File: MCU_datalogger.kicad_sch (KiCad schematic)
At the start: 25 parts, among them U1 24LC1025, U2 24LC1025, U3 DS1337S_, U4 ATMEGA328P-AU, Y1 32.768 KHz, Y2 16 MHz

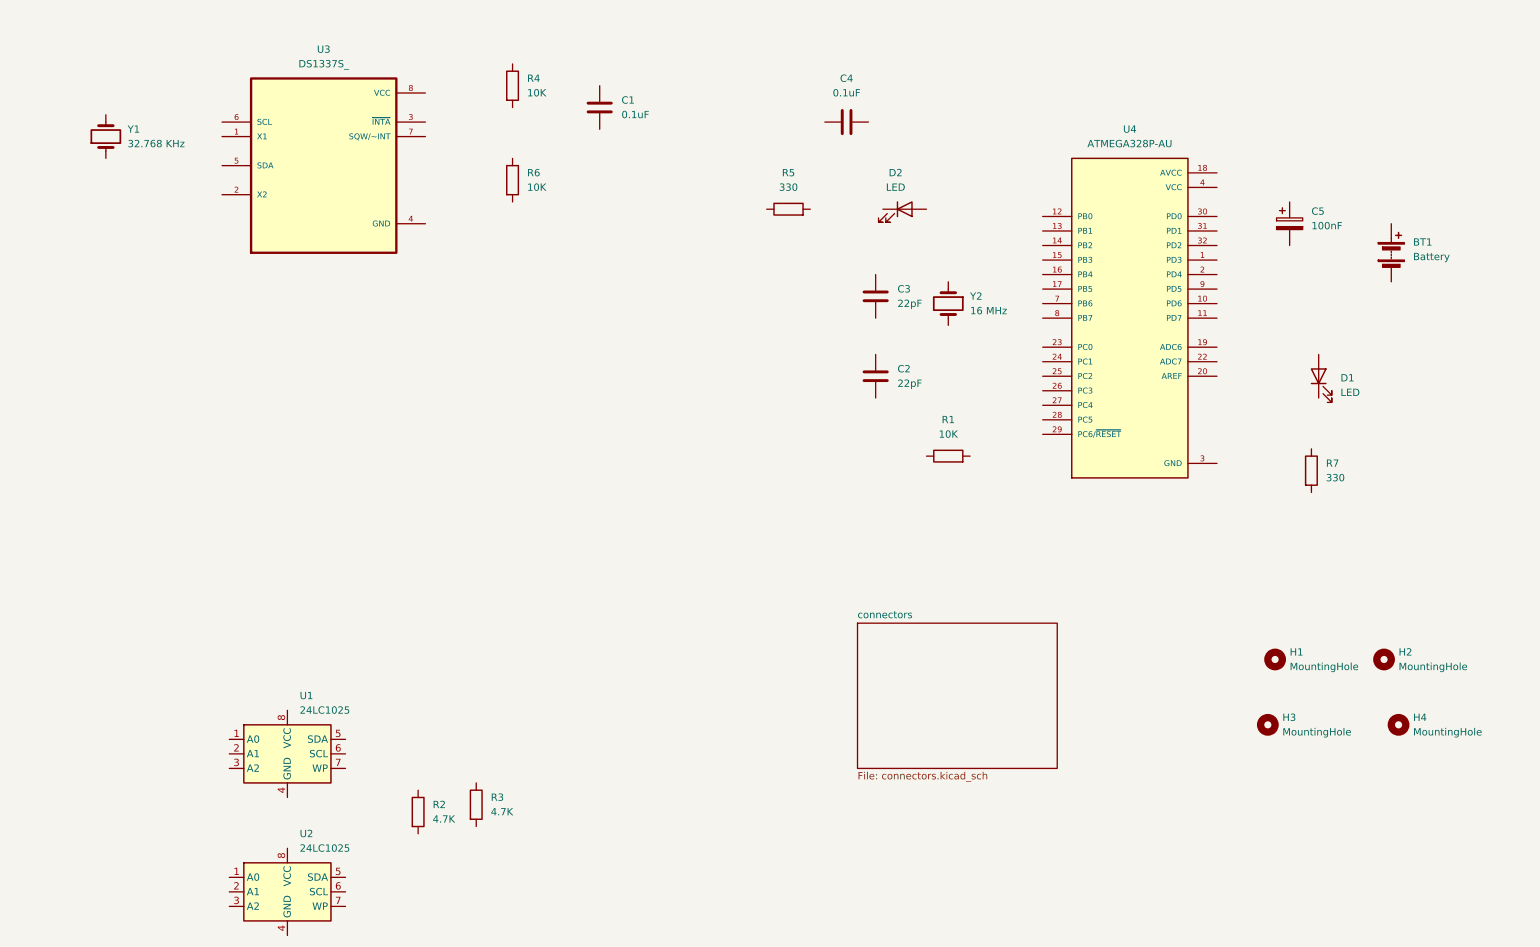
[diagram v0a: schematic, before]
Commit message: finished wiring main sheet
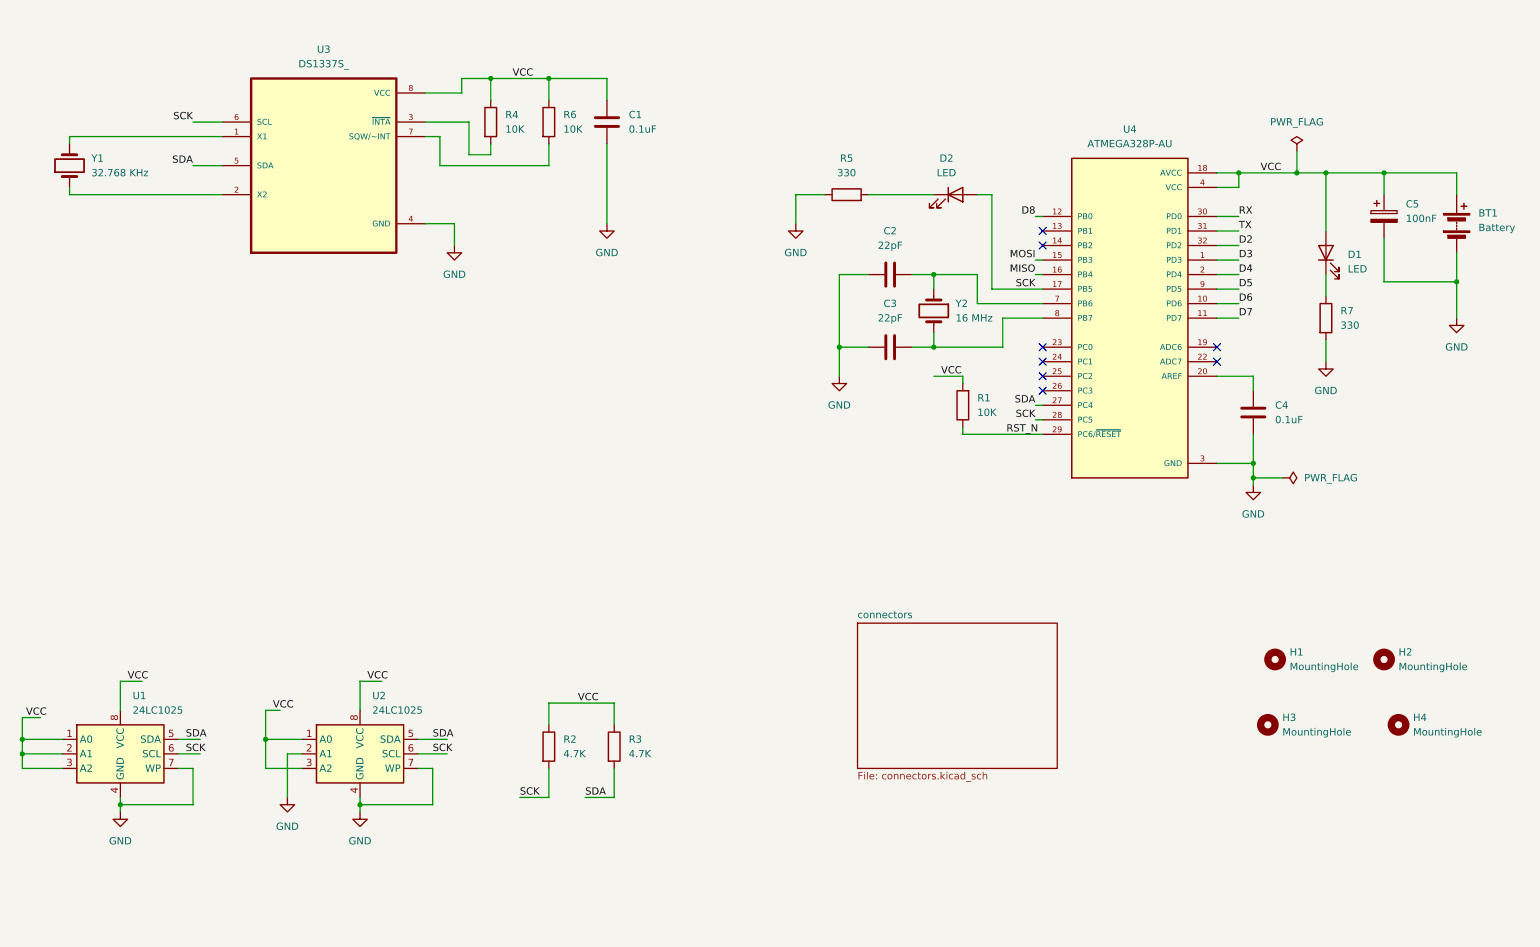
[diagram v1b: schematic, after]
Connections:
- net GND: now also BT1.2 (-), C1.2, C2.1, C3.1, C4.1, C5.2, R5.1, R7.2, U1.4 (GND), U1.7 (WP), U2.2 (A1), U2.4 (GND), U2.7 (WP), U3.4 (GND)
- net VCC: now also BT1.1 (+), C1.1, C5.1, D1.2 (A), R1.2, R2.1, R3.1, R4.1, R6.1, U1.1 (A0), U1.2 (A1), U1.3 (A2), U1.8 (VCC), U2.1 (A0), U2.3 (A2), U2.8 (VCC), U3.8 (VCC), U4.18 (AVCC)
- net SDA: now reaches R3.2
- net SDA: now also U1.5 (SDA), U2.5 (SDA), U3.5 (SDA), U4.27 (PC4)
- net RST_N: now reaches R1.1
- net RST_N: now also U4.29 (PC6/~{RESET})
- net SCK: now reaches R2.2
- net SCK: now also D2.2 (A), U1.6 (SCL), U2.6 (SCL), U3.6 (SCL), U4.17 (PB5), U4.28 (PC5)
- net at D1.1 (K): now also R7.1
- net at C2.2: now also U4.7 (PB6), Y2.1
- net at U3.1 (X1): now also Y1.2
- net at U3.2 (X2): now also Y1.1
- net at U3.3 (~{INTA}): now also R4.2
- net at U3.7 (SQW/~INT): now also R6.2
- net at C4.2: now also U4.20 (AREF)
- net at Y2.2: now also C3.2, U4.8 (PB7)
- net at D2.1 (K): now also R5.2
- net D3: now reaches U4.1 (PD3)
- net D6: now reaches U4.10 (PD6)
- net D7: now reaches U4.11 (PD7)
- net D8: now reaches U4.12 (PB0)
- net MOSI: now reaches U4.15 (PB3)
- net MISO: now reaches U4.16 (PB4)
- net D4: now reaches U4.2 (PD4)
- net RX: now reaches U4.30 (PD0)
- net TX: now reaches U4.31 (PD1)
- net D2: now reaches U4.32 (PD2)
- net D5: now reaches U4.9 (PD5)
- no-connect marks 0 -> 8
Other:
- moved on the sheet: BT1, C1, C2, C3, C4, C5, D1, D2, R1, R2, R3, R4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

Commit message: finished wiring connector sheet
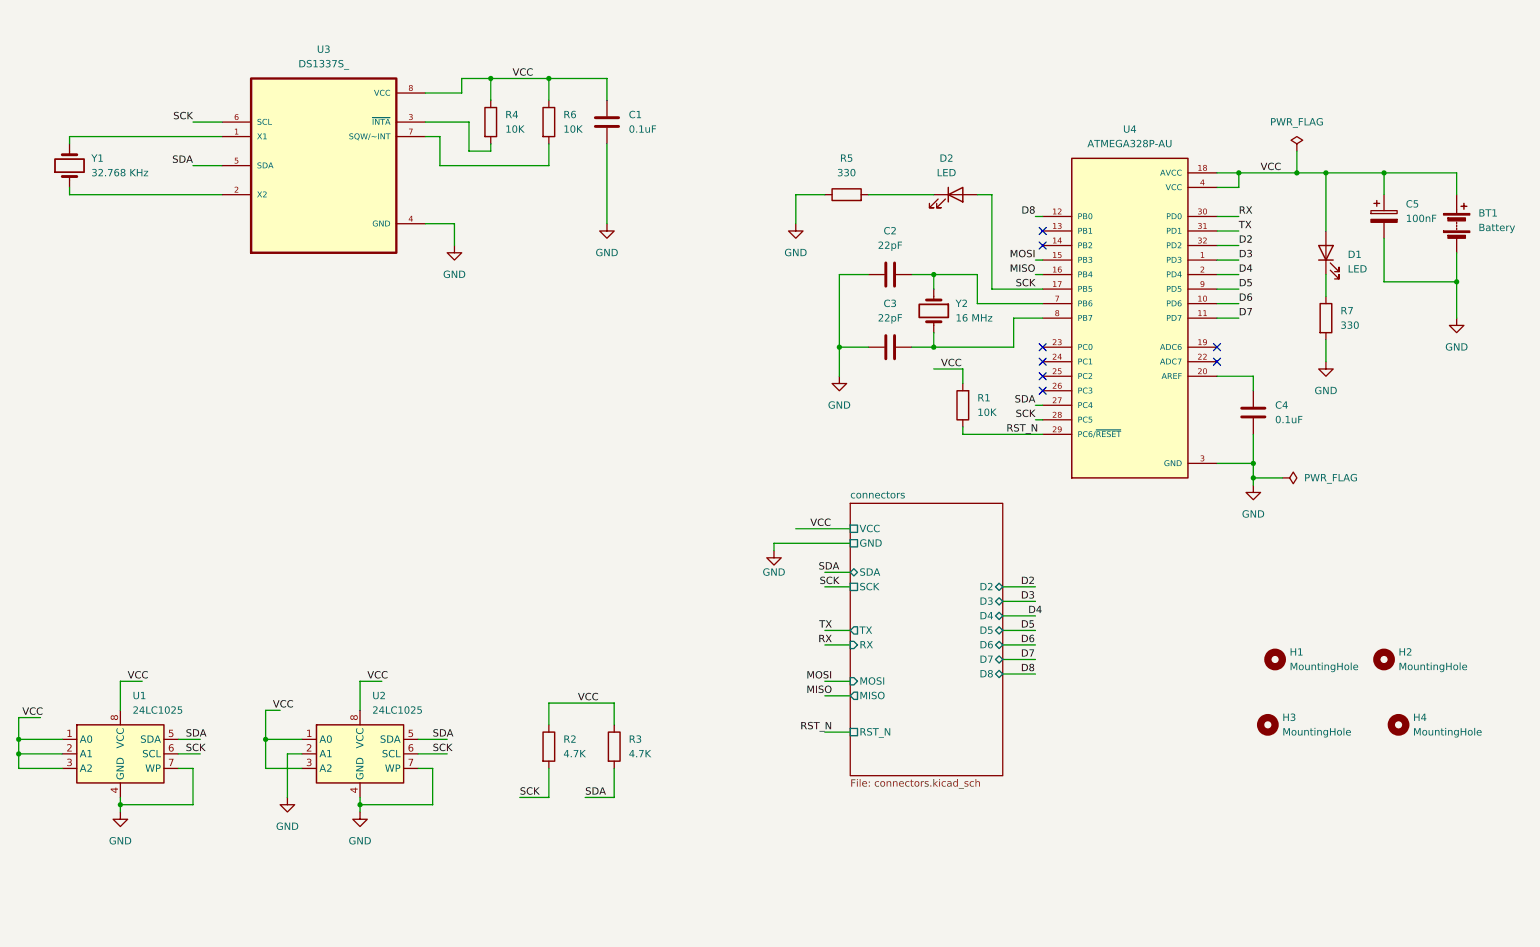
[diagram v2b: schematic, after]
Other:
- sheet connectors ports: added D2, D3, D4, D5, D6, D7, D8, GND, MISO, MOSI, RST_N, RX, SCK, SDA, TX, VCC; removed none

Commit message: added schematic comments
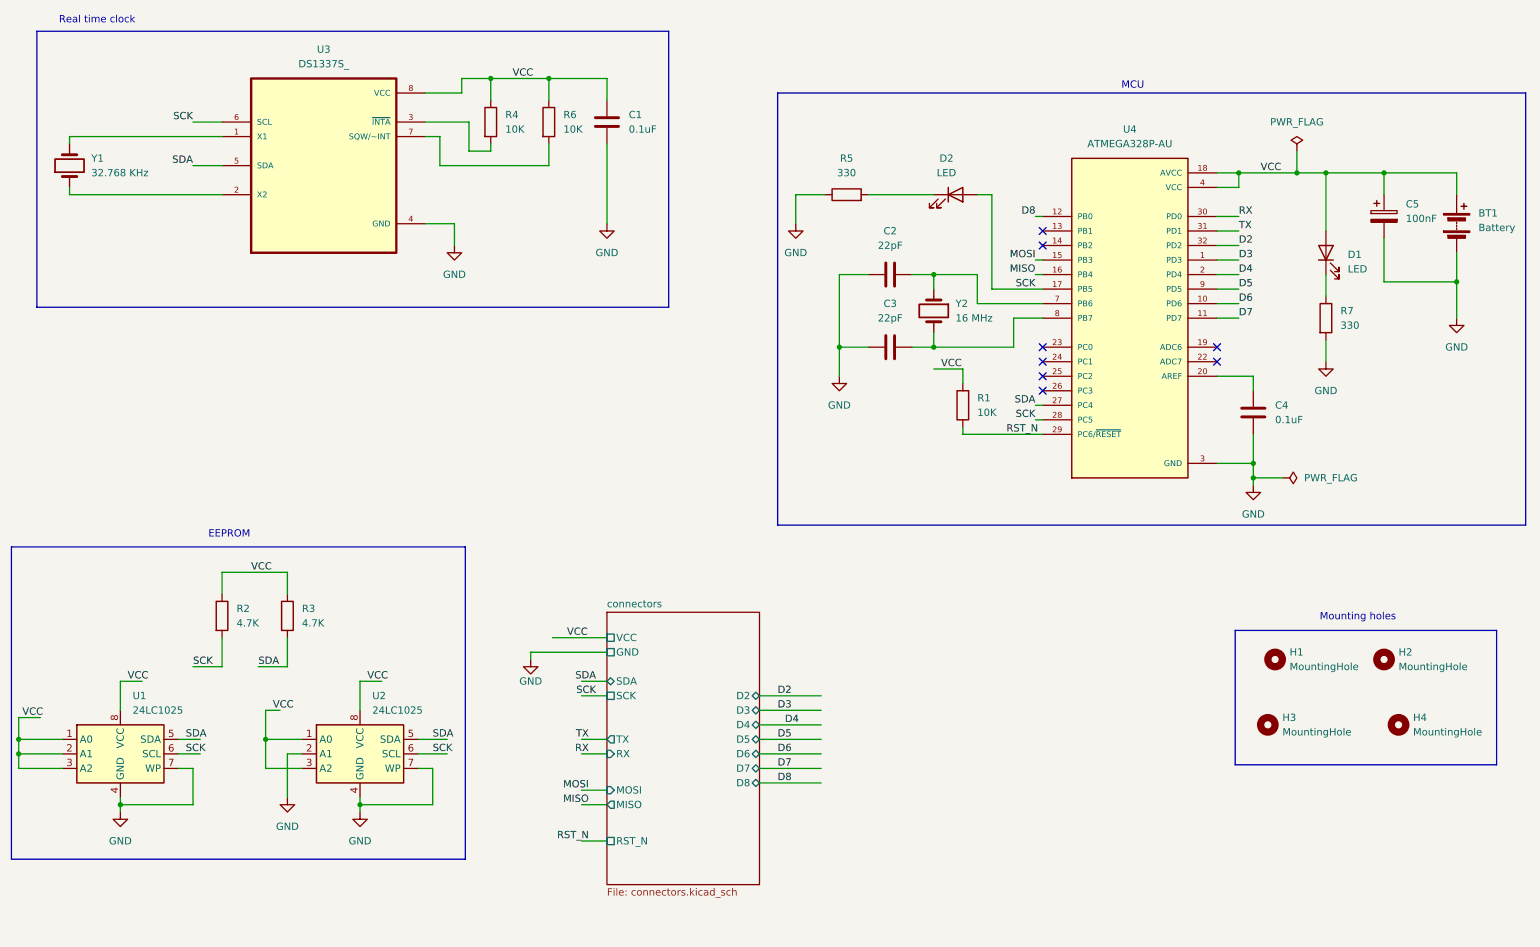
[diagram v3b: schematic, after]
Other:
- note added: "EEPROM"
- note added: "MCU"
- note added: "Mounting holes"
- note added: "Real time clock"
- moved on the sheet: R2, R3

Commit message: placed footprints and made edge cut
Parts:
- renumbered D2 to D1, D1 to D2, R4 to R1, R6 to R2, R2 to R3, R3 to R4, R1 to R6, U3 to U2, U2 to U3
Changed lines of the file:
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@@
 		(dnp no)
 		(fields_autoplaced yes)
-		(property "Reference" "R3"
+		(property "Reference" "R4"
 			(at 66.04 130.8099 0)
 			(show_name no)
@@
 			(project "MCU_datalogger"
 				(path "/755fa3e0-2b76-4b1a-a49f-069f1564984c"
-					(reference "R3")
+					(reference "R4")
 					(unit 1)
 				)
@@
 		(dnp no)
 		(fields_autoplaced yes)
-		(property "Reference" "R1"
+		(property "Reference" "R6"
 			(at 184.15 93.9799 0)
 			(show_name no)
@@
 			(project "MCU_datalogger"
 				(path "/755fa3e0-2b76-4b1a-a49f-069f1564984c"
-					(reference "R1")
+					(reference "R6")
 					(unit 1)
 				)
@@
 		(dnp no)
 		(fields_autoplaced yes)
-		(property "Reference" "R2"
+		(property "Reference" "R3"
 			(at 54.61 130.8099 0)
 			(show_name no)
@@
 			(project "MCU_datalogger"
 				(path "/755fa3e0-2b76-4b1a-a49f-069f1564984c"
-					(reference "R2")
+					(reference "R3")
 					(unit 1)
 				)
@@
 		(dnp no)
 		(fields_autoplaced yes)
-		(property "Reference" "D1"
+		(property "Reference" "D2"
 			(at 248.92 68.8974 90)
 			(show_name no)
@@
 			(project "MCU_datalogger"
 				(path "/755fa3e0-2b76-4b1a-a49f-069f1564984c"
-					(reference "D1")
+					(reference "D2")
 					(unit 1)
 				)
@@
 		(dnp no)
 		(fields_autoplaced yes)
-		(property "Reference" "U3"
+		(property "Reference" "U2"
 			(at 69.85 33.02 0)
 			(show_name no)
@@
 			(project "MCU_datalogger"
 				(path "/755fa3e0-2b76-4b1a-a49f-069f1564984c"
-					(reference "U3")
+					(reference "U2")
 					(unit 1)
 				)
@@
 		(dnp no)
 		(fields_autoplaced yes)
-		(property "Reference" "D2"
+		(property "Reference" "D1"
 			(at 178.7525 52.07 0)
 			(show_name no)
@@
 			(project "MCU_datalogger"
 				(path "/755fa3e0-2b76-4b1a-a49f-069f1564984c"
-					(reference "D2")
+					(reference "D1")
 					(unit 1)
 				)
@@
 		(dnp no)
 		(fields_autoplaced yes)
-		(property "Reference" "R6"
+		(property "Reference" "R2"
 			(at 111.76 44.4499 0)
 			(show_name no)
@@
 			(project "MCU_datalogger"
 				(path "/755fa3e0-2b76-4b1a-a49f-069f1564984c"
-					(reference "R6")
+					(reference "R2")
 					(unit 1)
 				)
@@
 		(dnp no)
 		(fields_autoplaced yes)
-		(property "Reference" "U2"
+		(property "Reference" "U3"
 			(at 78.3433 146.05 0)
 			(show_name no)
@@
 			(project "MCU_datalogger"
 				(path "/755fa3e0-2b76-4b1a-a49f-069f1564984c"
-					(reference "U2")
+					(reference "U3")
 					(unit 1)
 				)
@@
 		(dnp no)
 		(fields_autoplaced yes)
-		(property "Reference" "R4"
+		(property "Reference" "R1"
 			(at 101.6 44.4499 0)
 			(show_name no)
@@
 			(project "MCU_datalogger"
 				(path "/755fa3e0-2b76-4b1a-a49f-069f1564984c"
-					(reference "R4")
+					(reference "R1")
 					(unit 1)
 				)

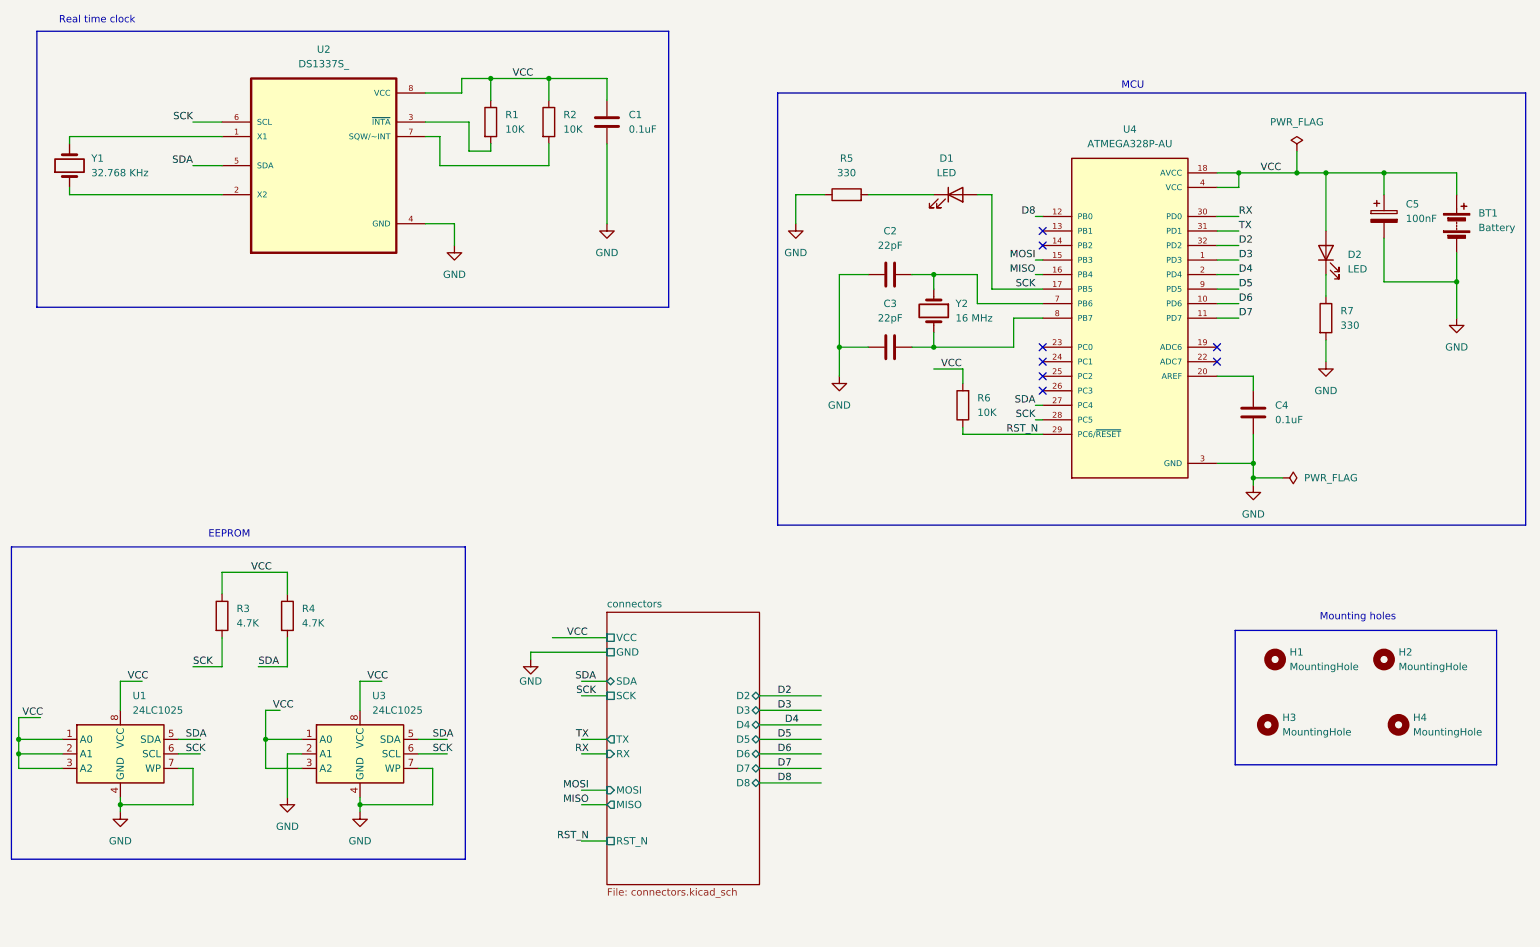
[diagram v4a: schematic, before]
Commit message: fixed scl and sck bug in schematic
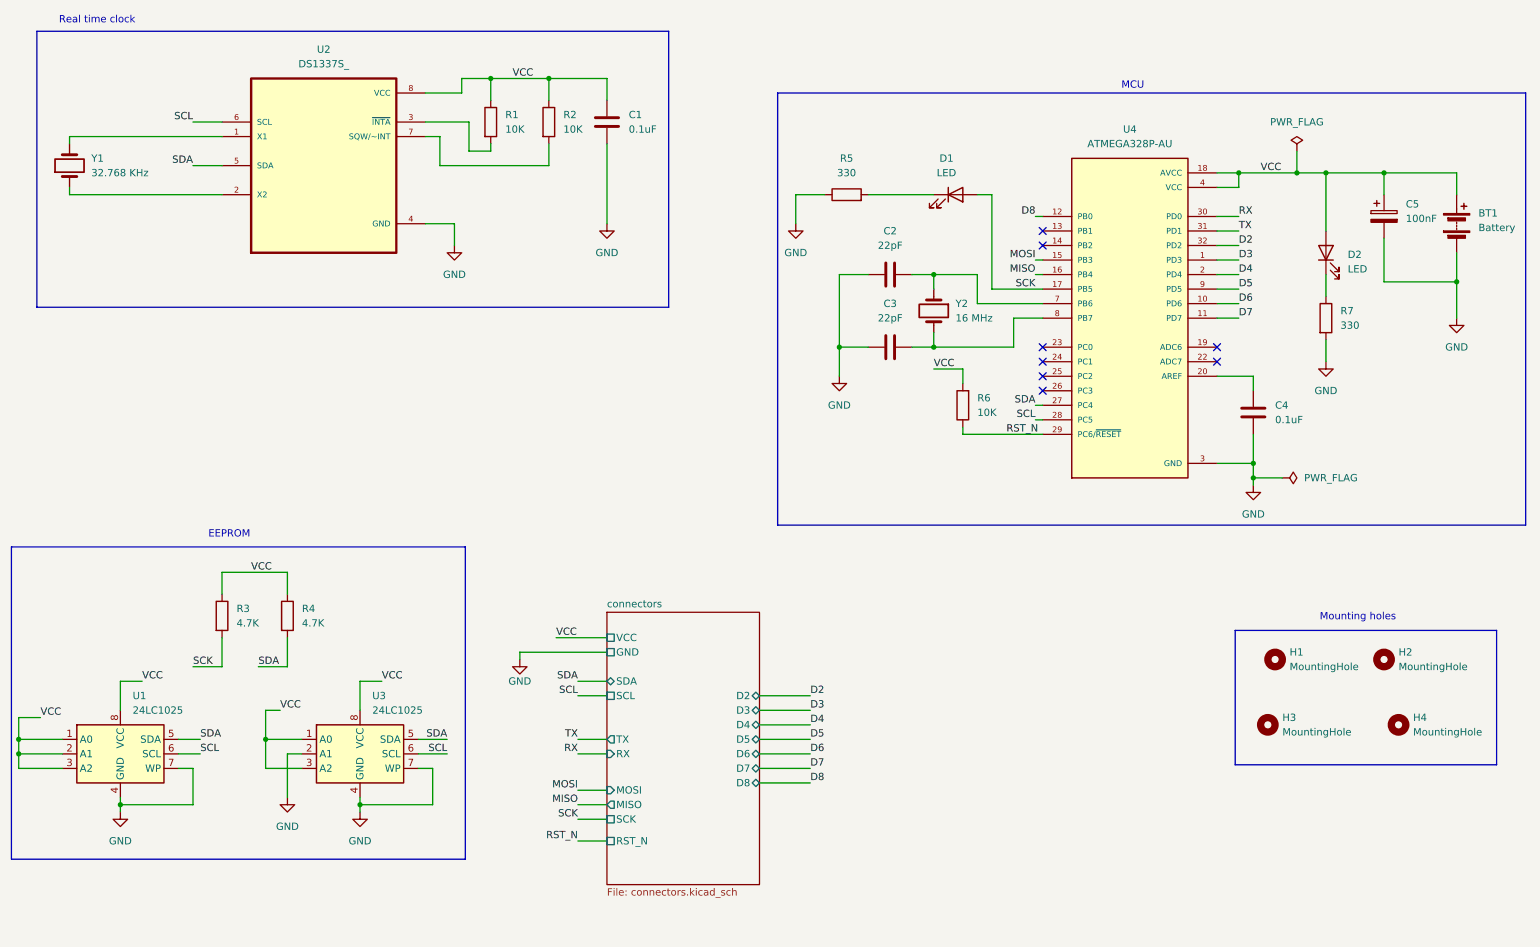
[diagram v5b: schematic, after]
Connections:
- net SCK: no longer U1.6 (SCL), U2.6 (SCL), U3.6 (SCL), U4.28 (PC5)
- new net SCL: U1.6 (SCL), U2.6 (SCL), U3.6 (SCL), U4.28 (PC5)
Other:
- sheet connectors ports: added SCL; removed none
